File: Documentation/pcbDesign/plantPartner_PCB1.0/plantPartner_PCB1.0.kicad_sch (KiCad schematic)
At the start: 69 parts, among them IC1 MPM3610, J1 Conn_01x04, J10 Screw_Terminal_01x03, J11 Conn_01x04, J12 Conn_01x03, J13 Conn_01x03, J14 Conn_01x03, J15 Conn_01x03, J16 Conn_01x04, J17 Conn_01x03, J18 Screw_Terminal_01x02, J19 Barrel_Jack, J2 Conn_01x04, J20 Conn_02x04_Top_Bottom, J3 Conn_01x04, J4 Screw_Terminal, J5 Conn_01x02, J6 Screw_Terminal_01x03, J7 Conn_01x03, J8 Conn_02x04_Top_Bottom, J9 Conn_01x03, K1 SRD-05VDC-SL-C, K2 SRD-05VDC-SL-C, Q1 PNP, Q2 PNP, U1 EL357N-G, U2 MAX485, U3 ESP32-DEVKIT-V1, U4 EL357N-G

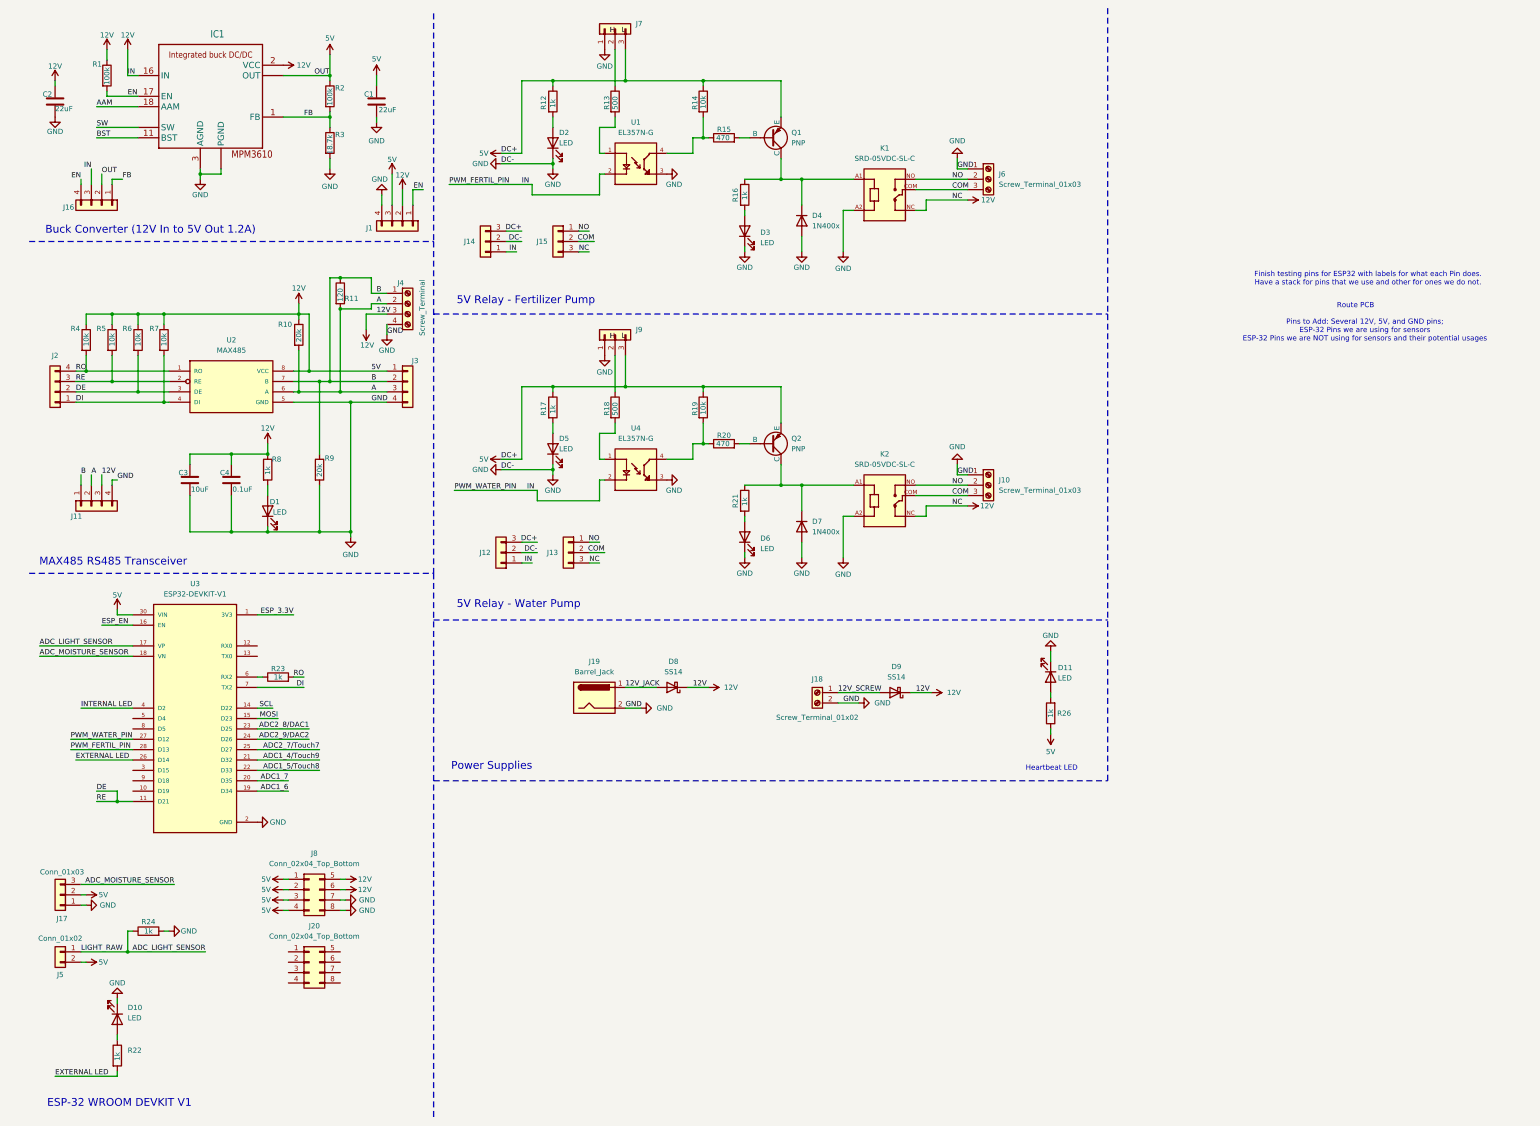
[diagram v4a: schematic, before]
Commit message: Finished adding Testing Pins. Starting Routing by drawing it out and organizing components in PCB. Quickly realized that I incorrectly setup 5V and 12V labels so will need to re-label those soon
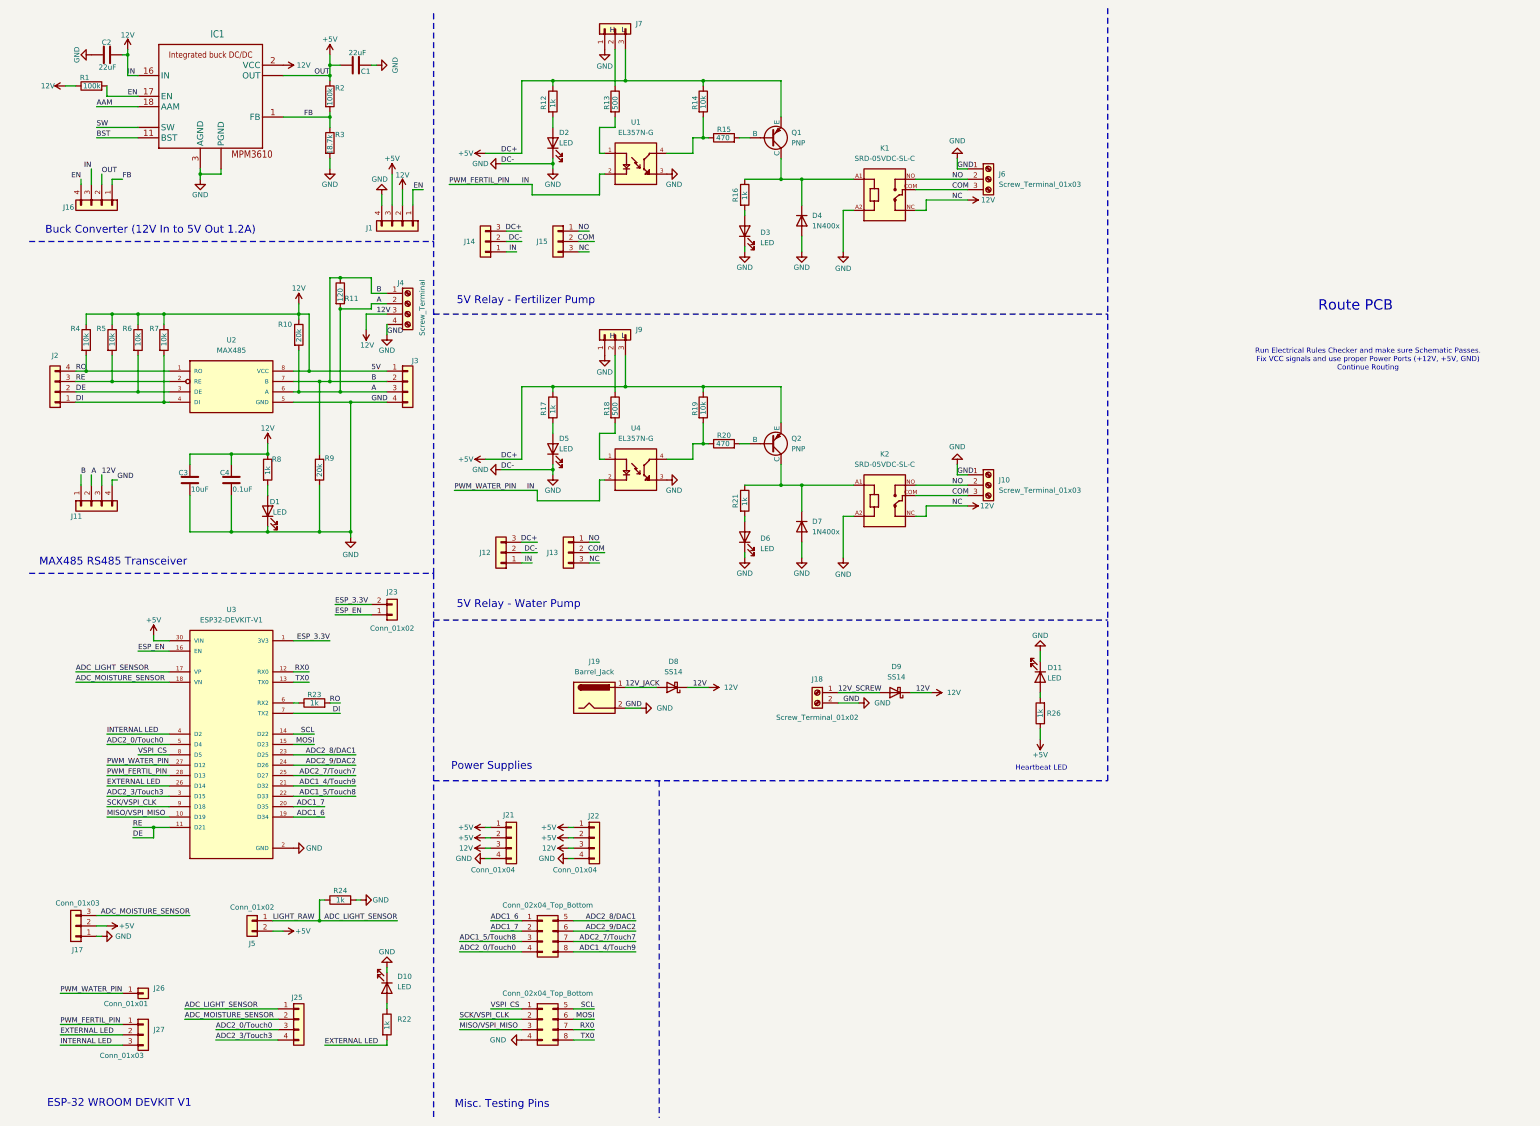
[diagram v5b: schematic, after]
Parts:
- added J21, J22, J25: Conn_01x04, Connector_PinHeader_2.54mm:PinHeader_1x04_P2.54mm_Vertical, symbol Connector_Generic:Conn_01x04
- added J23: Conn_01x02, Connector_PinHeader_2.54mm:PinHeader_1x02_P2.54mm_Vertical, symbol Connector_Generic:Conn_01x02
- added J26: Conn_01x01, Connector_PinHeader_2.54mm:PinHeader_1x01_P2.54mm_Vertical, symbol Connector_Generic:Conn_01x01
- added J27: Conn_01x03, Connector_PinHeader_2.54mm:PinHeader_1x03_P2.54mm_Vertical, symbol Connector_Generic:Conn_01x03
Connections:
- net 12V: now also J21.3 (Pin_3), J22.3 (Pin_3), J26.1 (Pin_1), J27.1 (Pin_1); no longer C1.1, IC1.7 (OUT), IC1.8 (OUT), IC1.9 (OUT), J1.3 (Pin_3), J12.3 (Pin_3), J14.3 (Pin_3), J16.2 (Pin_2), J17.2 (Pin_2), J5.2 (Pin_2), J7.3 (Pin_3), J8.1 (Pin_1), J8.2 (Pin_2), J8.3 (Pin_3), J8.4 (Pin_4), J8.5 (Pin_5), J8.6 (Pin_6), J9.3 (Pin_3), Q1.3 (E), Q2.3 (E), R12.1, R14.1, R17.1, R19.1, R2.1, R26.1, U3.30 (VIN)
- net ADC1_4/Touch9: now also J20.8 (Pin_8)
- net ADC1_5/Touch8: now also J20.3 (Pin_3)
- net ADC1_6: now also J20.1 (Pin_1)
- net ADC1_7: now also J20.2 (Pin_2)
- net ADC2_7/Touch7: now also J20.7 (Pin_7)
- net ADC2_8/DAC1: now also J20.5 (Pin_5)
- net ADC2_9/DAC2: now also J20.6 (Pin_6)
- net ADC_LIGHT_SENSOR: now also J25.1 (Pin_1)
- net ADC_MOISTURE_SENSOR: now also J25.2 (Pin_2)
- net ESP_3.3V: now also J23.2 (Pin_2)
- net ESP_EN: now also J23.1 (Pin_1)
- net EXTERNAL LED: now also J27.2 (Pin_2)
- net GND: now also J8.4 (Pin_4), J21.4 (Pin_4), J22.4 (Pin_4); no longer J8.7 (Pin_7), J8.8 (Pin_8)
- net INTERNAL LED: now also J27.3 (Pin_3)
- net MOSI: now also J8.6 (Pin_6)
- net SCL: now also J8.5 (Pin_5)
- net MISO/VSPI_MISO: now reaches U3.10 (D19)
- net MISO/VSPI_MISO: now also J8.3 (Pin_3)
- net RX0: now reaches U3.12 (RX0)
- net RX0: now also J8.7 (Pin_7)
- net TX0: now reaches U3.13 (TX0)
- net TX0: now also J8.8 (Pin_8)
- net at U3.3 (D15): no longer names the net of U3.3 (D15)
- net at U3.3 (D15): now also J25.4 (Pin_4)
- net ADC2_0/Touch0: now reaches U3.5 (D4)
- net ADC2_0/Touch0: now also J20.4 (Pin_4), J25.3 (Pin_3)
- net VSPI_CS: now reaches U3.8 (D5)
- net VSPI_CS: now also J8.1 (Pin_1)
- net SCK/VSPI_CLK: now reaches U3.9 (D18)
- net SCK/VSPI_CLK: now also J8.2 (Pin_2)
- new net +5V: C1.1, IC1.7 (OUT), IC1.8 (OUT), IC1.9 (OUT), J1.3 (Pin_3), J12.3 (Pin_3), J14.3 (Pin_3), J16.2 (Pin_2), J17.2 (Pin_2), J21.1 (Pin_1), J21.2 (Pin_2), J22.1 (Pin_1), J22.2 (Pin_2), J5.2 (Pin_2), J7.3 (Pin_3), J9.3 (Pin_3), Q1.3 (E), Q2.3 (E), R12.1, R14.1, R17.1, R19.1, R2.1, R26.1, U3.30 (VIN)
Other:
- note added: "Misc. Testing Pins"
- note added: "Run Electrical Rules Checker and make sure Schematic Passes. Fix VCC signals and use proper Power Ports (+12V, +5V, GND) Continue Routing"
- note removed: "Finish testing pins for ESP32 with labels for what each Pin does. Have a stack for pins that we use and other for ones we do not."
- note removed: "Pins to Add: Several 12V, 5V, and GND pins; ESP-32 Pins we are using for sensors ESP-32 Pins we are NOT using for sensors and their potential usages"
- moved on the sheet: C1, C2, D10, D11, J17, J5, R1, R22, R23, R24, R26, U3

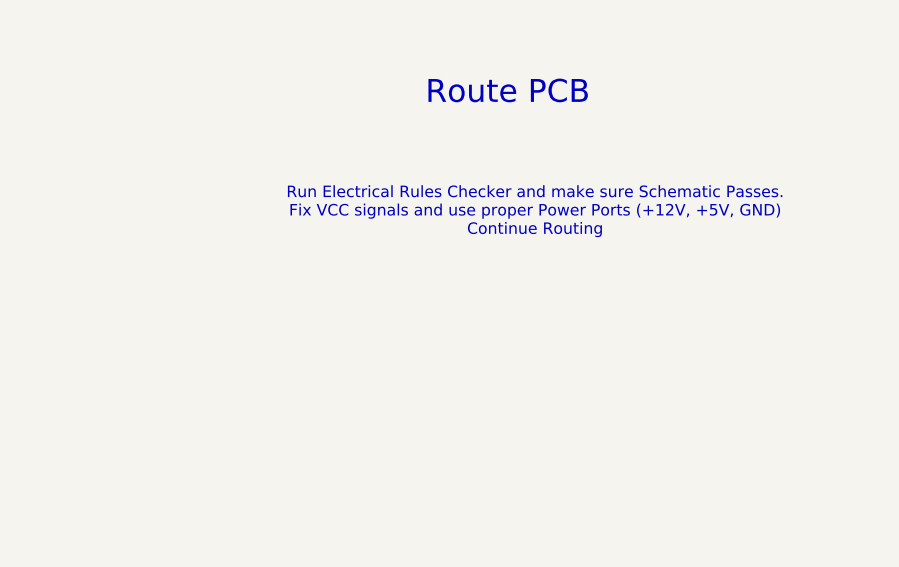
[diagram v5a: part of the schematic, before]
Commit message: Added a small note to schematic
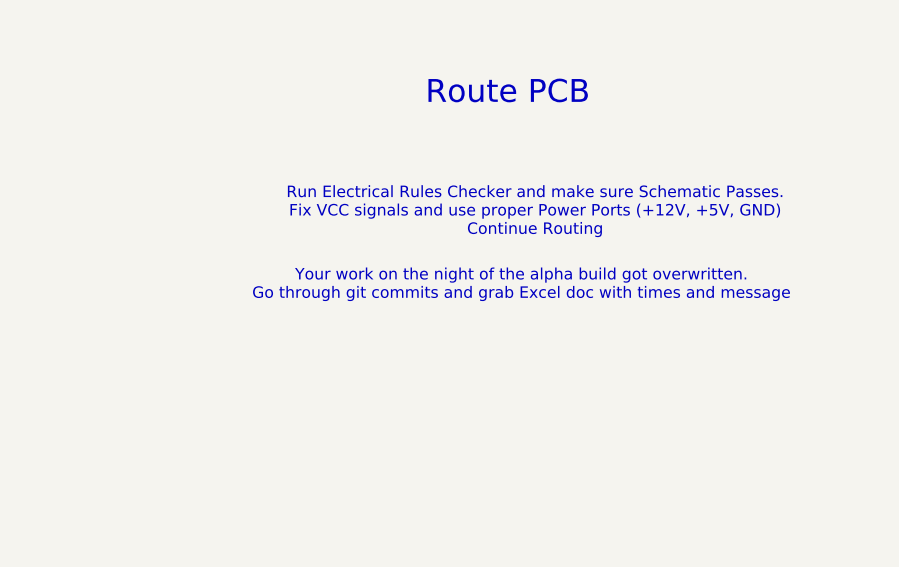
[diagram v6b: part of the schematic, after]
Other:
- note added: "Your work on the night of the alpha build got overwritten. Go through git commits and grab Excel doc with times and message"
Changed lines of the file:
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@@
+		)
+	)
+	(text "Your work on the night of the alpha build got overwritten. \nGo through git commits and grab Excel doc with times and message"
+		(exclude_from_sim no)
+		(at 339.09 106.934 0)
+		(effects
+			(font
+				(size 1.27 1.27)
+			)
 		)
 	)

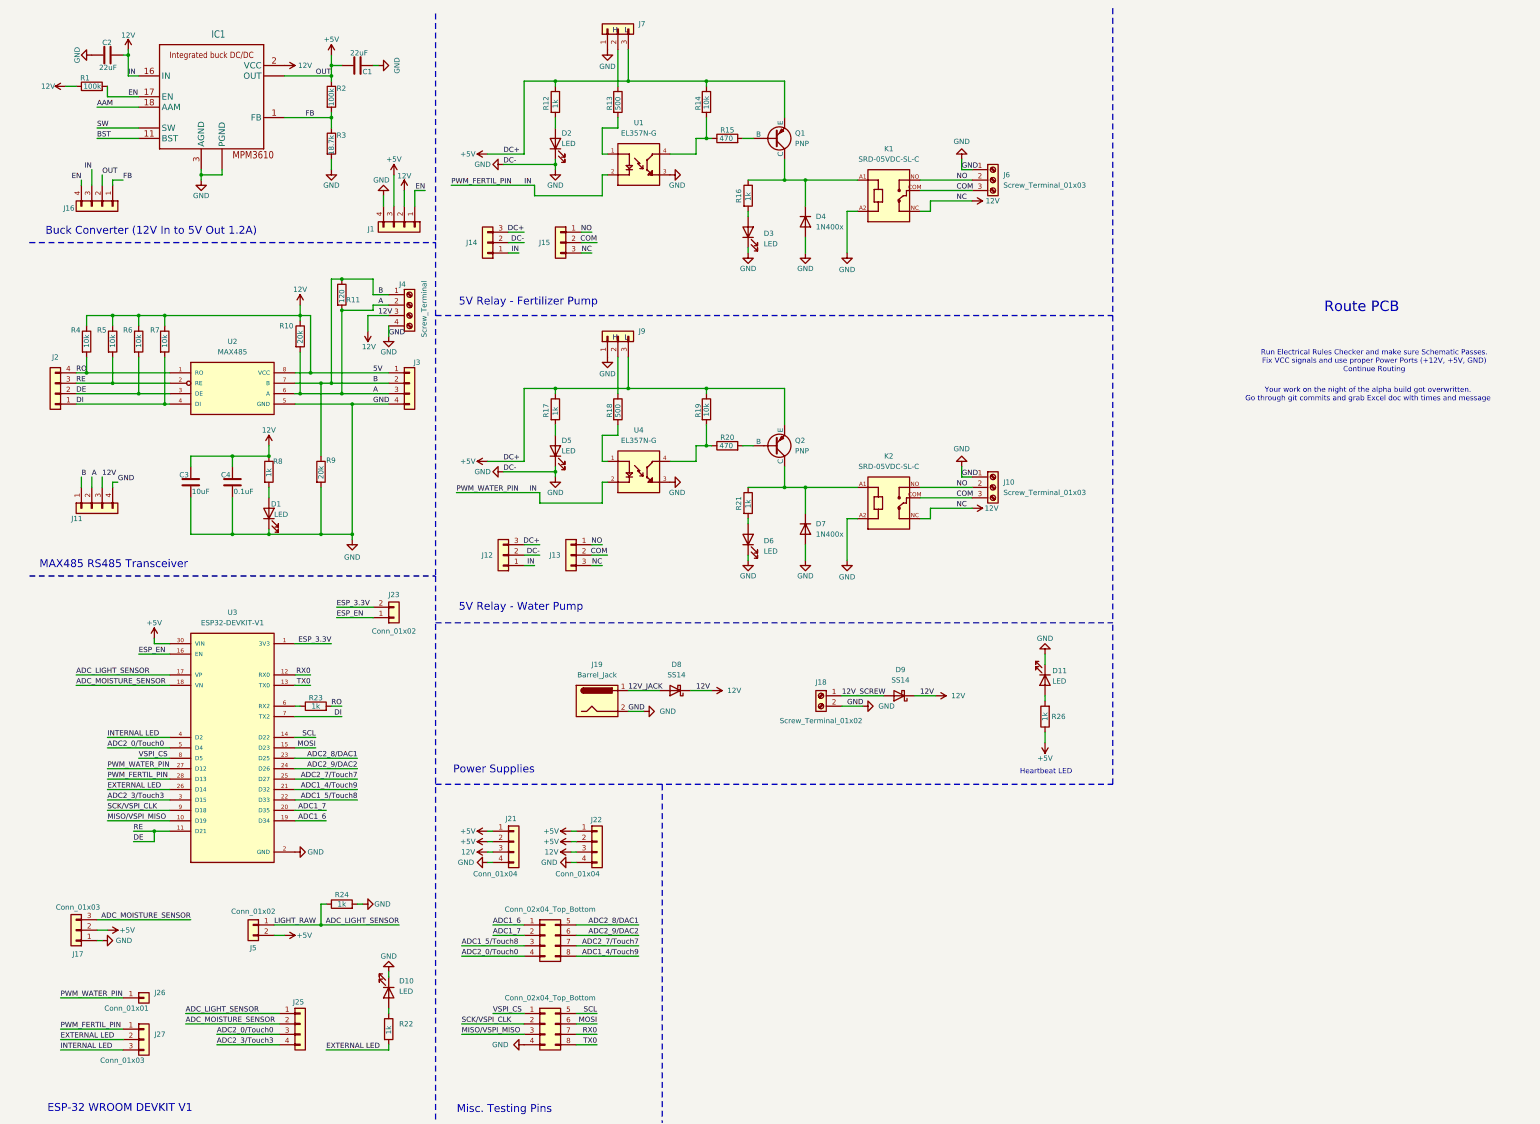
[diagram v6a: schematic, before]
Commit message: We showed off the Alpha Build to Tyler and I worked on the PCB Routing. I am trying to resolve the Electrical Rules Checker (ERC) now while routing.
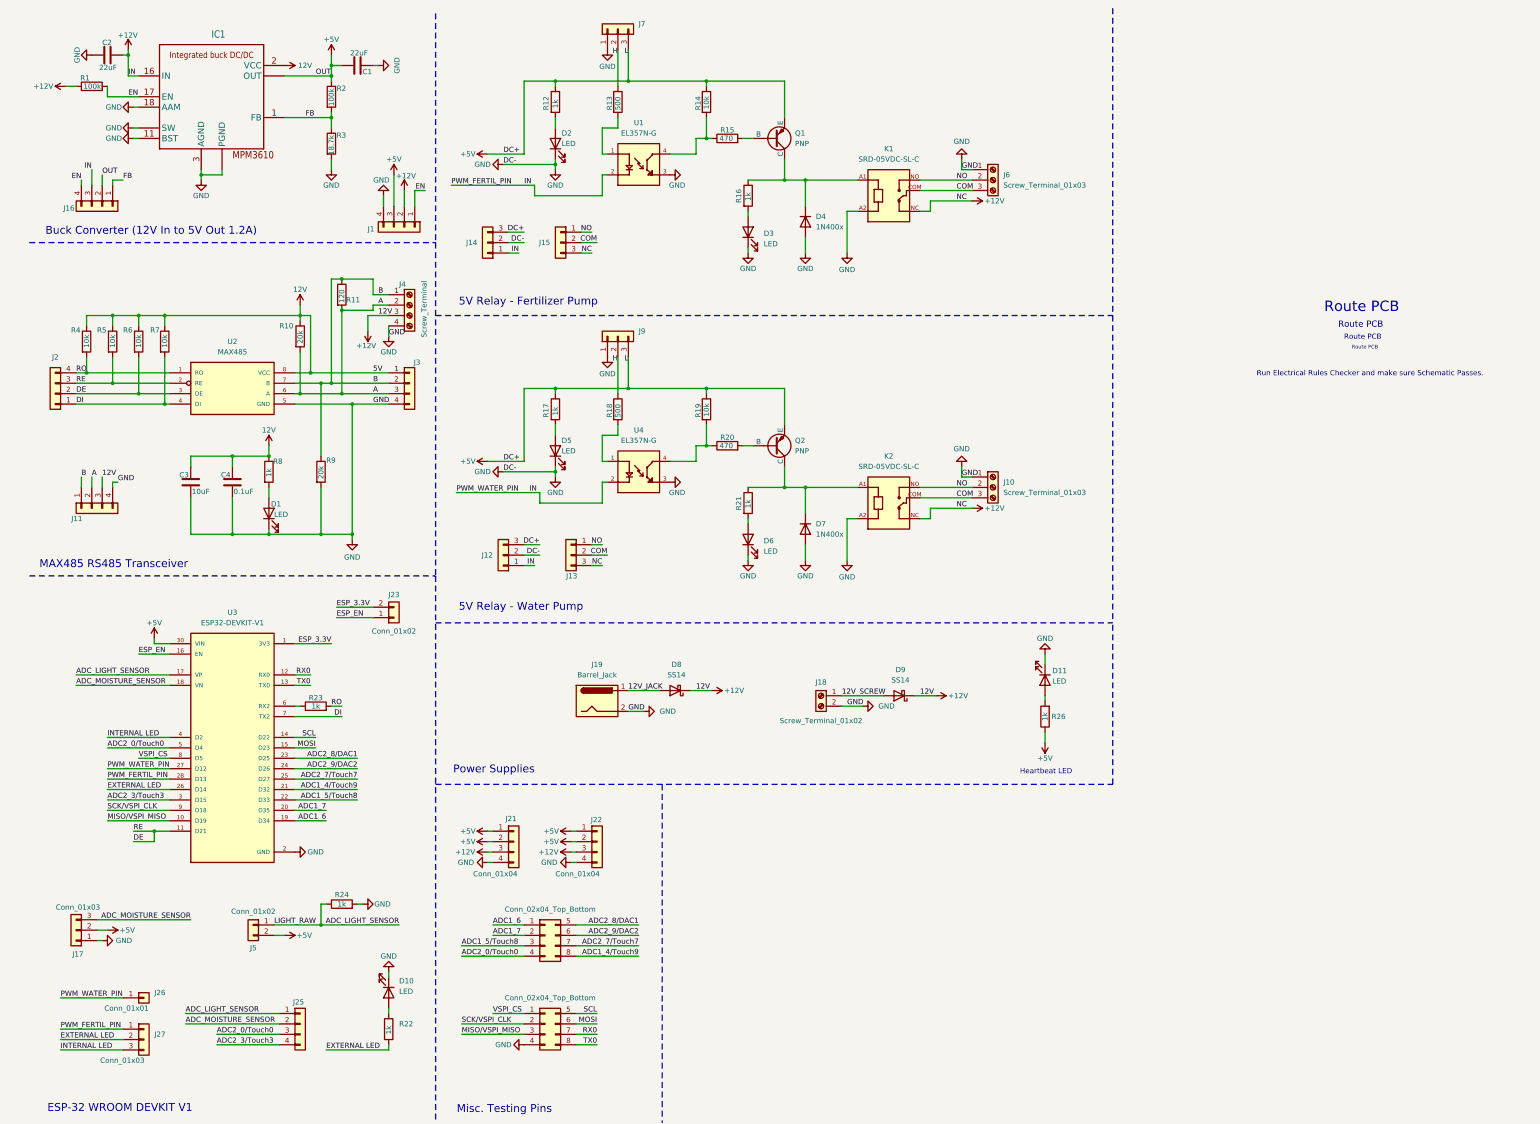
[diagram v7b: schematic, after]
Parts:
- IC1: footprint MyCustomFootprints:MPM3610 -> buckConverter:MPM3610
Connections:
- net AAM is gone; now on net GND: IC1.18 (AAM)
- net BST is gone; now on net GND: IC1.11 (BST)
- net SW is gone; now on net GND: IC1.4 (SW), IC1.5 (SW), IC1.6 (SW)
- net H: now also J7.2 (Pin_2), J9.2 (Pin_2), R13.1, R18.1
- net ADC2_3/Touch3: now reaches J25.4 (Pin_4), U3.3 (D15)
- net 12V renamed +12V
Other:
- note added: "Run Electrical Rules Checker and make sure Schematic Passes."
- note removed: "Run Electrical Rules Checker and make sure Schematic Passes. Fix VCC signals and use proper Power Ports (+12V, +5V, GND) Continue Routing"
- note removed: "Your work on the night of the alpha build got overwritten. Go through git commits and grab Excel doc with times and message"
